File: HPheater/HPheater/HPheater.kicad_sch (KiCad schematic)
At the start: 2 parts

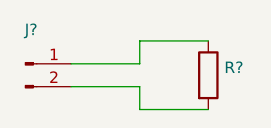
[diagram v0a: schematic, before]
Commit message: started heater layout.  need to make heater smaller to accomodate some kind of mounting holes, need to add mounting for controller
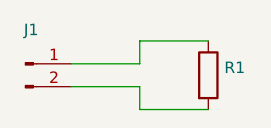
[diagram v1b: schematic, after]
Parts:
- gave numbers to parts that had none: 2
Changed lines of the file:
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@@
   (symbol (lib_id "Device:R") (at 107.95 62.23 0) (unit 1)
     (in_bom yes) (on_board yes) (fields_autoplaced)
-    (property "Reference" "R?" (id 0) (at 109.728 61.3953 0)
+    (property "Reference" "R1" (id 0) (at 109.728 61.3953 0)
       (effects (font (size 1.27 1.27)) (justify left))
     )
@@
   (symbol (lib_id "Connector:Conn_01x02_Male") (at 87.63 60.96 0) (unit 1)
     (in_bom yes) (on_board yes) (fields_autoplaced)
-    (property "Reference" "J?" (id 0) (at 88.265 57.184 0))
+    (property "Reference" "J1" (id 0) (at 88.265 57.184 0))
     (property "Value" "" (id 1) (at 88.265 59.7209 0))
     (property "Footprint" "" (id 2) (at 87.63 60.96 0)
@@
   (symbol_instances
     (path "/c1c799a0-3c93-493a-9ad7-8a0561bc69ee"
-      (reference "J?") (unit 1) (value "Conn_01x02_Male") (footprint "")
+      (reference "J1") (unit 1) (value "Conn_01x02_Male") (footprint "connector_custom:AMASS_XT60PW-F")
     )
     (path "/020b7e1f-8bb0-4882-91d4-7894bf18db84"
-      (reference "R?") (unit 1) (value "R") (footprint "")
+      (reference "R1") (unit 1) (value "R") (footprint "Resistor_SMD:R_1206_3216Metric_Pad1.30x1.75mm_HandSolder")
     )
   )

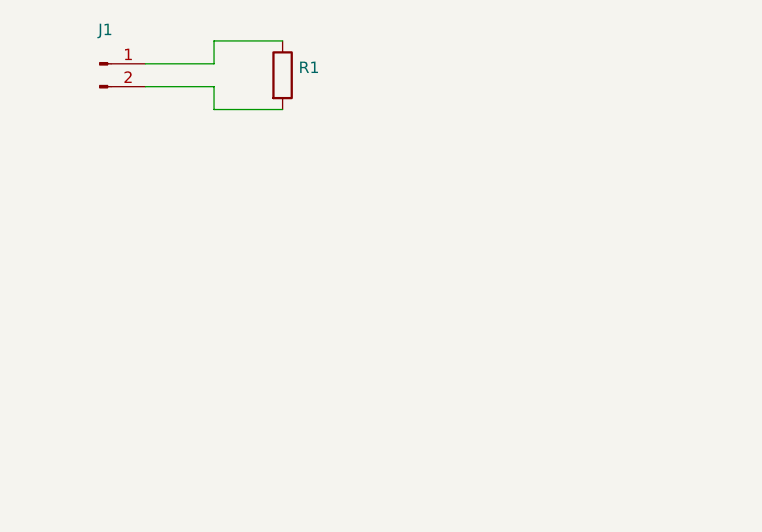
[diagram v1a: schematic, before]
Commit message: changed heater size, added mounting, refined slot
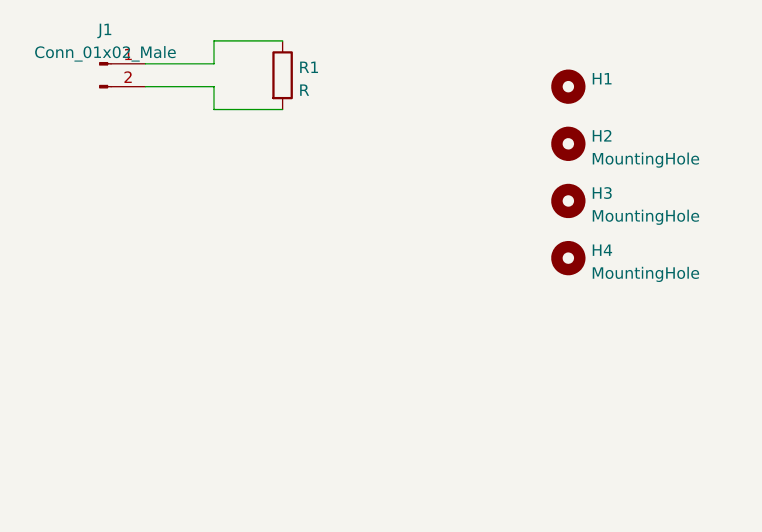
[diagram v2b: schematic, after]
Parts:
- added H1: (no value), symbol Mechanical:MountingHole
- added H2, H3, H4: MountingHole, symbol Mechanical:MountingHole
- J1: value (none) -> Conn_01x02_Male; footprint (none) -> connector_custom:AMASS_XT60PW-F
- R1: value (none) -> R; footprint (none) -> Resistor_SMD:R_1206_3216Metric_Pad1.30x1.75mm_HandSolder
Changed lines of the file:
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@@
       (effects (font (size 1.27 1.27)) (justify left))
     )
-    (property "Value" "" (id 1) (at 109.728 63.9322 0)
+    (property "Value" "R" (id 1) (at 109.728 63.9322 0)
       (effects (font (size 1.27 1.27)) (justify left))
     )
-    (property "Footprint" "" (id 2) (at 106.172 62.23 90)
+    (property "Footprint" "Resistor_SMD:R_1206_3216Metric_Pad1.30x1.75mm_HandSolder" (id 2) (at 106.172 62.23 90)
       (effects (font (size 1.27 1.27)) hide)
     )
@@
     (pin "2")
   )
+  (symbol (lib_id "Mechanical:MountingHole") (at 139.7 76.2 0) (unit 1)
+    (in_bom yes) (on_board yes) (fields_autoplaced)
+    (property "Reference" "H3" (id 0) (at 142.24 75.3653 0)
+      (effects (font (size 1.27 1.27)) (justify left))
+    )
+    (property "Value" "MountingHole" (id 1) (at 142.24 77.9022 0)
+      (effects (font (size 1.27 1.27)) (justify left))
+    )
+    (property "Footprint" "" (id 2) (at 139.7 76.2 0)
+      (effects (font (size 1.27 1.27)) hide)
+    )
+    (property "Datasheet" "~" (id 3) (at 139.7 76.2 0)
+      (effects (font (size 1.27 1.27)) hide)
+    )
+  )
+  (symbol (lib_id "Mechanical:MountingHole") (at 139.7 69.85 0) (unit 1)
+    (in_bom yes) (on_board yes) (fields_autoplaced)
+    (property "Reference" "H2" (id 0) (at 142.24 69.0153 0)
+      (effects (font (size 1.27 1.27)) (justify left))
+    )
+    (property "Value" "MountingHole" (id 1) (at 142.24 71.5522 0)
+      (effects (font (size 1.27 1.27)) (justify left))
+    )
+    (property "Footprint" "" (id 2) (at 139.7 69.85 0)
+      (effects (font (size 1.27 1.27)) hide)
+    )
+    (property "Datasheet" "~" (id 3) (at 139.7 69.85 0)
+      (effects (font (size 1.27 1.27)) hide)
+    )
+  )
+  (symbol (lib_id "Mechanical:MountingHole") (at 139.7 63.5 0) (unit 1)
+    (in_bom yes) (on_board yes) (fields_autoplaced)
+    (property "Reference" "H1" (id 0) (at 142.24 62.6653 0)
+      (effects (font (size 1.27 1.27)) (justify left))
+    )
+    (property "Value" "" (id 1) (at 142.24 65.2022 0)
+      (effects (font (size 1.27 1.27)) (justify left))
+    )
+    (property "Footprint" "" (id 2) (at 139.7 63.5 0)
+      (effects (font (size 1.27 1.27)) hide)
+    )
+    (property "Datasheet" "~" (id 3) (at 139.7 63.5 0)
+      (effects (font (size 1.27 1.27)) hide)
+    )
+  )
+  (symbol (lib_id "Mechanical:MountingHole") (at 139.7 82.55 0) (unit 1)
+    (in_bom yes) (on_board yes) (fields_autoplaced)
+    (property "Reference" "H4" (id 0) (at 142.24 81.7153 0)
+      (effects (font (size 1.27 1.27)) (justify left))
+    )
+    (property "Value" "MountingHole" (id 1) (at 142.24 84.2522 0)
+      (effects (font (size 1.27 1.27)) (justify left))
+    )
+    (property "Footprint" "" (id 2) (at 139.7 82.55 0)
+      (effects (font (size 1.27 1.27)) hide)
+    )
+    (property "Datasheet" "~" (id 3) (at 139.7 82.55 0)
+      (effects (font (size 1.27 1.27)) hide)
+    )
+  )
   (symbol (lib_id "Connector:Conn_01x02_Male") (at 87.63 60.96 0) (unit 1)
     (in_bom yes) (on_board yes) (fields_autoplaced)
     (property "Reference" "J1" (id 0) (at 88.265 57.184 0))
-    (property "Value" "" (id 1) (at 88.265 59.7209 0))
-    (property "Footprint" "" (id 2) (at 87.63 60.96 0)
+    (property "Value" "Conn_01x02_Male" (id 1) (at 88.265 59.7209 0))
+    (property "Footprint" "connector_custom:AMASS_XT60PW-F" (id 2) (at 87.63 60.96 0)
       (effects (font (size 1.27 1.27)) hide)
     )
@@
   )
   (symbol_instances
+    (path "/4fb21471-41be-4be8-9687-66030f97befc"
+      (reference "H1") (unit 1) (value "MountingHole") (footprint "MountingHole:MountingHole_2.2mm_M2_ISO14580")
+    )
+    (path "/4ab287b0-f7e5-4d54-ac56-3885f4c05418"
+      (reference "H2") (unit 1) (value "MountingHole") (footprint "MountingHole:MountingHole_2.2mm_M2_ISO14580")
+    )
+    (path "/32f708e0-df94-44e7-a6ae-cda54a0cd338"
+      (reference "H3") (unit 1) (value "MountingHole") (footprint "MountingHole:MountingHole_2.2mm_M2_ISO14580")
+    )
+    (path "/a7928873-604e-41b4-8f3c-a9332a26491c"
+      (reference "H4") (unit 1) (value "MountingHole") (footprint "MountingHole:MountingHole_2.2mm_M2_ISO14580")
+    )
     (path "/c1c799a0-3c93-493a-9ad7-8a0561bc69ee"
       (reference "J1") (unit 1) (value "Conn_01x02_Male") (footprint "connector_custom:AMASS_XT60PW-F")

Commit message: finished routing heater
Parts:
- H1: value (none) -> MountingHole; footprint (none) -> MountingHole:MountingHole_2.5mm
- H2, H3, H4: footprint (none) -> MountingHole:MountingHole_2.5mm
- J1: footprint connector_custom:AMASS_XT60PW-F -> HPfootprint:HEATER_CONTACT
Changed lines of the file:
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@@
-(kicad_sch (version 20211123) (generator eeschema)
+(kicad_sch (version 20230121) (generator eeschema)
   (paper "A4")
   (wire (pts (xy 100.33 60.96) (xy 100.33 58.42))
-    (stroke (width 0) (type default) (color 0 0 0 0))
+    (stroke (width 0) (type default))
   )
   (wire (pts (xy 100.33 58.42) (xy 107.95 58.42))
-    (stroke (width 0) (type default) (color 0 0 0 0))
+    (stroke (width 0) (type default))
   )
   (wire (pts (xy 100.33 66.04) (xy 107.95 66.04))
-    (stroke (width 0) (type default) (color 0 0 0 0))
+    (stroke (width 0) (type default))
   )
   (wire (pts (xy 92.71 60.96) (xy 100.33 60.96))
-    (stroke (width 0) (type default) (color 0 0 0 0))
+    (stroke (width 0) (type default))
   )
   (wire (pts (xy 100.33 63.5) (xy 100.33 66.04))
-    (stroke (width 0) (type default) (color 0 0 0 0))
+    (stroke (width 0) (type default))
   )
   (wire (pts (xy 92.71 63.5) (xy 100.33 63.5))
-    (stroke (width 0) (type default) (color 0 0 0 0))
+    (stroke (width 0) (type default))
   )
   (symbol (lib_id "Device:R") (at 107.95 62.23 0) (unit 1)
-    (in_bom yes) (on_board yes) (fields_autoplaced)
-    (property "Reference" "R1" (id 0) (at 109.728 61.3953 0)
+    (in_bom yes) (on_board yes) (dnp no) (fields_autoplaced)
+    (property "Reference" "R1" (at 109.728 61.3953 0)
       (effects (font (size 1.27 1.27)) (justify left))
     )
-    (property "Value" "R" (id 1) (at 109.728 63.9322 0)
+    (property "Value" "R" (at 109.728 63.9322 0)
       (effects (font (size 1.27 1.27)) (justify left))
     )
-    (property "Footprint" "Resistor_SMD:R_1206_3216Metric_Pad1.30x1.75mm_HandSolder" (id 2) (at 106.172 62.23 90)
+    (property "Footprint" "Resistor_SMD:R_1206_3216Metric_Pad1.30x1.75mm_HandSolder" (at 106.172 62.23 90)
       (effects (font (size 1.27 1.27)) hide)
     )
-    (property "Datasheet" "~" (id 3) (at 107.95 62.23 0)
+    (property "Datasheet" "~" (at 107.95 62.23 0)
       (effects (font (size 1.27 1.27)) hide)
     )
     (pin "1")
     (pin "2")
+    (instances
+      (project "HPheater"
+        (path "/e63e39d7-6ac0-4ffd-8aa3-1841a4541b55"
+          (reference "R1") (unit 1)
+        )
+      )
+    )
   )
   (symbol (lib_id "Mechanical:MountingHole") (at 139.7 76.2 0) (unit 1)
-    (in_bom yes) (on_board yes) (fields_autoplaced)
-    (property "Reference" "H3" (id 0) (at 142.24 75.3653 0)
+    (in_bom yes) (on_board yes) (dnp no) (fields_autoplaced)
+    (property "Reference" "H3" (at 142.24 75.3653 0)
       (effects (font (size 1.27 1.27)) (justify left))
     )
-    (property "Value" "MountingHole" (id 1) (at 142.24 77.9022 0)
+    (property "Value" "MountingHole" (at 142.24 77.9022 0)
       (effects (font (size 1.27 1.27)) (justify left))
     )
-    (property "Footprint" "" (id 2) (at 139.7 76.2 0)
+    (property "Footprint" "MountingHole:MountingHole_2.5mm" (at 139.7 76.2 0)
       (effects (font (size 1.27 1.27)) hide)
     )
-    (property "Datasheet" "~" (id 3) (at 139.7 76.2 0)
+    (property "Datasheet" "~" (at 139.7 76.2 0)
       (effects (font (size 1.27 1.27)) hide)
+    )
+    (instances
+      (project "HPheater"
+        (path "/e63e39d7-6ac0-4ffd-8aa3-1841a4541b55"
+          (reference "H3") (unit 1)
+        )
+      )
     )
   )
   (symbol (lib_id "Mechanical:MountingHole") (at 139.7 69.85 0) (unit 1)
-    (in_bom yes) (on_board yes) (fields_autoplaced)
-    (property "Reference" "H2" (id 0) (at 142.24 69.0153 0)
+    (in_bom yes) (on_board yes) (dnp no) (fields_autoplaced)
+    (property "Reference" "H2" (at 142.24 69.0153 0)
       (effects (font (size 1.27 1.27)) (justify left))
     )
-    (property "Value" "MountingHole" (id 1) (at 142.24 71.5522 0)
+    (property "Value" "MountingHole" (at 142.24 71.5522 0)
       (effects (font (size 1.27 1.27)) (justify left))
     )
-    (property "Footprint" "" (id 2) (at 139.7 69.85 0)
+    (property "Footprint" "MountingHole:MountingHole_2.5mm" (at 139.7 69.85 0)
       (effects (font (size 1.27 1.27)) hide)
     )
-    (property "Datasheet" "~" (id 3) (at 139.7 69.85 0)
+    (property "Datasheet" "~" (at 139.7 69.85 0)
       (effects (font (size 1.27 1.27)) hide)
+    )
+    (instances
+      (project "HPheater"
+        (path "/e63e39d7-6ac0-4ffd-8aa3-1841a4541b55"
+          (reference "H2") (unit 1)
+        )
+      )
     )
   )
   (symbol (lib_id "Mechanical:MountingHole") (at 139.7 63.5 0) (unit 1)
-    (in_bom yes) (on_board yes) (fields_autoplaced)
-    (property "Reference" "H1" (id 0) (at 142.24 62.6653 0)
+    (in_bom yes) (on_board yes) (dnp no) (fields_autoplaced)
+    (property "Reference" "H1" (at 142.24 62.6653 0)
       (effects (font (size 1.27 1.27)) (justify left))
     )
-    (property "Value" "" (id 1) (at 142.24 65.2022 0)
+    (property "Value" "MountingHole" (at 142.24 65.2022 0)
       (effects (font (size 1.27 1.27)) (justify left))
     )
-    (property "Footprint" "" (id 2) (at 139.7 63.5 0)
+    (property "Footprint" "MountingHole:MountingHole_2.5mm" (at 139.7 63.5 0)
       (effects (font (size 1.27 1.27)) hide)
     )
-    (property "Datasheet" "~" (id 3) (at 139.7 63.5 0)
+    (property "Datasheet" "~" (at 139.7 63.5 0)
       (effects (font (size 1.27 1.27)) hide)
+    )
+    (instances
+      (project "HPheater"
+        (path "/e63e39d7-6ac0-4ffd-8aa3-1841a4541b55"
+          (reference "H1") (unit 1)
+        )
+      )
     )
   )
   (symbol (lib_id "Mechanical:MountingHole") (at 139.7 82.55 0) (unit 1)
-    (in_bom yes) (on_board yes) (fields_autoplaced)
-    (property "Reference" "H4" (id 0) (at 142.24 81.7153 0)
+    (in_bom yes) (on_board yes) (dnp no) (fields_autoplaced)
+    (property "Reference" "H4" (at 142.24 81.7153 0)
       (effects (font (size 1.27 1.27)) (justify left))
     )
-    (property "Value" "MountingHole" (id 1) (at 142.24 84.2522 0)
+    (property "Value" "MountingHole" (at 142.24 84.2522 0)
       (effects (font (size 1.27 1.27)) (justify left))
     )
-    (property "Footprint" "" (id 2) (at 139.7 82.55 0)
+    (property "Footprint" "MountingHole:MountingHole_2.5mm" (at 139.7 82.55 0)
       (effects (font (size 1.27 1.27)) hide)
     )
-    (property "Datasheet" "~" (id 3) (at 139.7 82.55 0)
+    (property "Datasheet" "~" (at 139.7 82.55 0)
       (effects (font (size 1.27 1.27)) hide)
+    )
+    (instances
+      (project "HPheater"
+        (path "/e63e39d7-6ac0-4ffd-8aa3-1841a4541b55"
+          (reference "H4") (unit 1)
+        )
+      )
     )
   )
   (symbol (lib_id "Connector:Conn_01x02_Male") (at 87.63 60.96 0) (unit 1)
-    (in_bom yes) (on_board yes) (fields_autoplaced)
-    (property "Reference" "J1" (id 0) (at 88.265 57.184 0))
-    (property "Value" "Conn_01x02_Male" (id 1) (at 88.265 59.7209 0))
-    (property "Footprint" "connector_custom:AMASS_XT60PW-F" (id 2) (at 87.63 60.96 0)
+    (in_bom yes) (on_board yes) (dnp no) (fields_autoplaced)
+    (property "Reference" "J1" (at 88.265 57.184 0)
+      (effects (font (size 1.27 1.27)))
+    )
+    (property "Value" "Conn_01x02_Male" (at 88.265 59.7209 0)
+      (effects (font (size 1.27 1.27)))
+    )
+    (property "Footprint" "HPfootprint:HEATER_CONTACT" (at 87.63 60.96 0)
       (effects (font (size 1.27 1.27)) hide)
     )
-    (property "Datasheet" "~" (id 3) (at 87.63 60.96 0)
+    (property "Datasheet" "~" (at 87.63 60.96 0)
       (effects (font (size 1.27 1.27)) hide)
     )
     (pin "1")
     (pin "2")
+    (instances
+      (project "HPheater"
+        (path "/e63e39d7-6ac0-4ffd-8aa3-1841a4541b55"
+          (reference "J1") (unit 1)
+        )
+      )
+    )
   )
   (sheet_instances
     (path "/" (page "1"))
   )
-  (symbol_instances
-    (path "/4fb21471-41be-4be8-9687-66030f97befc"
-      (reference "H1") (unit 1) (value "MountingHole") (footprint "MountingHole:MountingHole_2.2mm_M2_ISO14580")
-    )
-    (path "/4ab287b0-f7e5-4d54-ac56-3885f4c05418"
-      (reference "H2") (unit 1) (value "MountingHole") (footprint "MountingHole:MountingHole_2.2mm_M2_ISO14580")
-    )
-    (path "/32f708e0-df94-44e7-a6ae-cda54a0cd338"
-      (reference "H3") (unit 1) (value "MountingHole") (footprint "MountingHole:MountingHole_2.2mm_M2_ISO14580")
-    )
-    (path "/a7928873-604e-41b4-8f3c-a9332a26491c"
-      (reference "H4") (unit 1) (value "MountingHole") (footprint "MountingHole:MountingHole_2.2mm_M2_ISO14580")
-    )
-    (path "/c1c799a0-3c93-493a-9ad7-8a0561bc69ee"
-      (reference "J1") (unit 1) (value "Conn_01x02_Male") (footprint "connector_custom:AMASS_XT60PW-F")
-    )
-    (path "/020b7e1f-8bb0-4882-91d4-7894bf18db84"
-      (reference "R1") (unit 1) (value "R") (footprint "Resistor_SMD:R_1206_3216Metric_Pad1.30x1.75mm_HandSolder")
-    )
-  )
 )

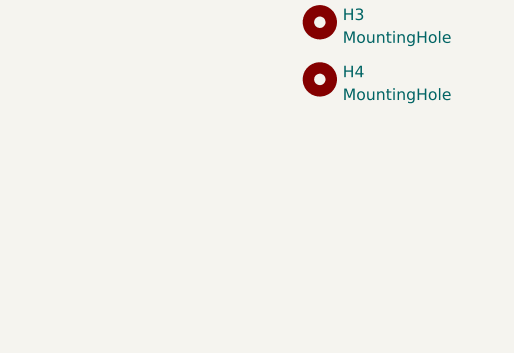
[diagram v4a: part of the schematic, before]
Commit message: fixed open on heater
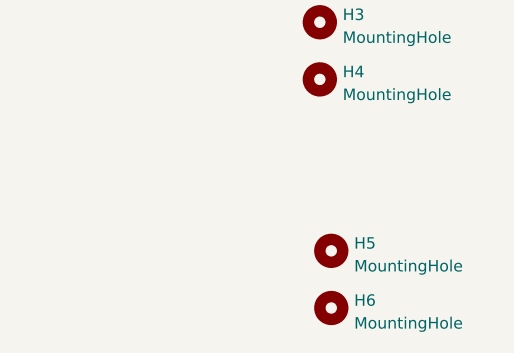
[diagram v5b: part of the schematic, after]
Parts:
- added H5, H6: MountingHole, MountingHole:MountingHole_2.7mm_M2.5, symbol Mechanical:MountingHole
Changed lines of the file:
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@@
+	(symbol
+		(lib_id "Mechanical:MountingHole")
+		(at 140.97 101.6 0)
+		(unit 1)
+		(exclude_from_sim no)
+		(in_bom yes)
+		(on_board yes)
+		(dnp no)
+		(fields_autoplaced yes)
+		(property "Reference" "H5"
+			(at 143.51 100.7653 0)
+			(effects
+				(font
+					(size 1.27 1.27)
+				)
+				(justify left)
+			)
+		)
+		(property "Value" "MountingHole"
+			(at 143.51 103.3022 0)
+			(effects
+				(font
+					(size 1.27 1.27)
+				)
+				(justify left)
+			)
+		)
+		(property "Footprint" "MountingHole:MountingHole_2.7mm_M2.5"
+			(at 140.97 101.6 0)
+			(effects
+				(font
+					(size 1.27 1.27)
+				)
+				(hide yes)
+			)
+		)
+		(property "Datasheet" "~"
+			(at 140.97 101.6 0)
+			(effects
+				(font
+					(size 1.27 1.27)
+				)
+				(hide yes)
+			)
+		)
+		(property "Description" ""
+			(at 140.97 101.6 0)
+			(effects
+				(font
+					(size 1.27 1.27)
+				)
+			)
+		)
+		(instances
+			(project "HPheater"
+				(path "/e63e39d7-6ac0-4ffd-8aa3-1841a4541b55"
+					(reference "H5")
+					(unit 1)
+				)
+			)
+		)
+	)
+	(symbol
+		(lib_id "Mechanical:MountingHole")
+		(at 140.97 107.95 0)
+		(unit 1)
+		(exclude_from_sim no)
+		(in_bom yes)
+		(on_board yes)
+		(dnp no)
+		(fields_autoplaced yes)
+		(property "Reference" "H6"
+			(at 143.51 107.1153 0)
+			(effects
+				(font
+					(size 1.27 1.27)
+				)
+				(justify left)
+			)
+		)
+		(property "Value" "MountingHole"
+			(at 143.51 109.6522 0)
+			(effects
+				(font
+					(size 1.27 1.27)
+				)
+				(justify left)
+			)
+		)
+		(property "Footprint" "MountingHole:MountingHole_2.7mm_M2.5"
+			(at 140.97 107.95 0)
+			(effects
+				(font
+					(size 1.27 1.27)
+				)
+				(hide yes)
+			)
+		)
+		(property "Datasheet" "~"
+			(at 140.97 107.95 0)
+			(effects
+				(font
+					(size 1.27 1.27)
+				)
+				(hide yes)
+			)
+		)
+		(property "Description" ""
+			(at 140.97 107.95 0)
+			(effects
+				(font
+					(size 1.27 1.27)
+				)
+			)
+		)
+		(instances
+			(project "HPheater"
+				(path "/e63e39d7-6ac0-4ffd-8aa3-1841a4541b55"
+					(reference "H6")
+					(unit 1)
+				)
+			)
+		)
+	)
 	(symbol
 		(lib_id "Mechanical:MountingHole")
